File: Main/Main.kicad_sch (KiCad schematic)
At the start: 39 parts, among them J1 USB_B_Micro, SW1 SW_Push, SW2 SW_Push, U1 RP2350A-QFN60, U2 W25Q128JVS, U3 AMS1117-3.3, Y1 ABM8-272-T3

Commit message: moveSchematics
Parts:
- added C22: 1u, symbol Device:C
- added C23: 10u, symbol Device:C
- added C24: 0.1, symbol Device:C
- added C25, C26: 0.1uF, symbol Device:C
- added C27, C28: 100 nF, symbol Device:C
- added D1, D2: 100nF, symbol Device:D_Capacitance
- added H5, H6, H7, H8: pad, symbol Mechanical:MountingHole
- added R10, R11, R12, R13, R14: 4.7k, symbol Device:R
- added R7, R8: R, symbol Device:R
- added R9: 2m, symbol Device:R_Shunt
- added U10: LM75B, symbol Sensor_Temperature:LM75B
- added U4: MMC5983MA, MMC5983MA_MEM, symbol MMC5983MA:MMC5983MA
- added U5: ICM-42688-P, ICM-42688-P:PQFN50P300X250X97-14N, symbol ICM-42688-P:ICM-42688-P
- added U6: INA226, Package_SO:VSSOP-10_3x3mm_P0.5mm, symbol Sensor_Energy:INA226
- added U7: KX134-1211, LGA12_2X2X0P9_ROM, symbol KX134:KX134-1211
- added U8: MS5611-01BA, Package_LGA:LGA-8_3x5mm_P1.25mm, symbol Sensor_Pressure:MS5611-01BA
- added U9: RP2350A, Package_DFN_QFN:QFN-60-1EP_7x7mm_P0.4mm_EP3.4x3.4mm, symbol MCU_RaspberryPi:RP2350A
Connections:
- net +3.3V: now also C22.1, C24.1, R10.1, R11.1, R12.1, U4.13 (VDDIO), U4.2 (VDD), U6.6 (VS)
- net GND: now also C22.2, C23.2, C24.2, C25.2, C26.1, C27.2, C28.2, D1.2 (A), D2.2 (A), R9.4, U10.4 (GND), U10.5 (A2), U10.6 (A1), U10.7 (A0), U4.11 (GND), U4.9 (GND), U5.6 (GND), U5.7 (RESV_7), U6.1 (A1), U6.2 (A0), U6.7 (GND), U7.8 (GND), U7.9 (GND), U8.2 (PS), U8.3 (GND), U9.47 (VREG_PGND), U9.61 (GND)
- new net: R7.1, U5.14 (AP_SDA/AP_SDIO/AP_SDI)
- new net: D2.1 (K), R7.2, R8.2, U5.10 (RESV_10), U5.12 (AP_CS), U5.2 (RESV_2), U5.3 (RESV_3), U5.5 (VDDIO)
- new net: R13.2, U10.1 (SDA), U9.7 (GPIO4)
- new net: C23.1, U4.10 (CAP)
- new net: R9.2, U6.10 (Vin+)
- new net: R9.3, U6.8 (Vbus), U6.9 (Vin-)
- new net: D1.1 (K), U5.8 (VDD)
- new net: R8.1, U5.13 (AP_SCL/AP_SCLK)
- new net: R14.2, U10.2 (SCL), U9.8 (GPIO5)
- new net: U9.1 (IOVDD), U9.11 (IOVDD), U9.20 (IOVDD), U9.30 (IOVDD), U9.38 (IOVDD), U9.45 (IOVDD)
- new net: U9.23 (DVDD), U9.39 (DVDD), U9.6 (DVDD)
- new net +3V0: C27.1, U8.1 (VDD)
- new net +3V3: C28.1, R13.1, R14.1, U10.8 (+Vs), U9.49 (VREG_VIN)
- new net +7.5V: R9.1
- new net ACCEL_INT1: U7.5 (INT1)
- new net ACCEL_INT2: U7.6 (INT2)
- new net ACCEL_SCLK/SCL: U7.12 (SCLK/SCL)
- new net ACCEL_SDI/SDA: U7.2 (SDI/SDA)
- new net ACCEL_SDO/ADDR: U7.1 (SDO/ADDR)
- new net ACCEL_TRIG: U7.4 (TRIG)
- new net ACCEL_nCS: U7.10 (nCS)
- new net Alert: R12.2, U6.3 (~{Alert})
- new net Chip Select: U8.4 (CSB), U8.5 (CSB)
- new net I2C SCL: R11.2, U6.5 (SCL)
- new net I2C SDA: R10.2, U6.4 (SDA)
- new net IO_VDD: C25.1, U7.3 (IO_VDD)
- new net SCLK: U8.8 (SCLK)
- new net SCL/SPI_5CK: U4.1 (SCL/SPI_SCK)
- new net SDA/SPI_5DI: U4.16 (SDA/SPI_SDI)
- new net SDI: U8.7 (SDI/SDA)
- new net SDO: U8.6 (SDO)
- new net SPI_CS: U4.4 (SPI_CS)
- new net SPI_SD0: U4.5 (SPI_SDO)
- new net VDD: C26.2, U7.7 (VDD)

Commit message: Updated footprints
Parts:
- removed D1, D2: 100nF, symbol Device:D_Capacitance
- removed H5, H6, H7, H8: pad, symbol Mechanical:MountingHole
- removed R7, R8: R, symbol Device:R
- removed U5: ICM-42688-P, ICM-42688-P:PQFN50P300X250X97-14N, symbol ICM-42688-P:ICM-42688-P
- removed U9: RP2350A, Package_DFN_QFN:QFN-60-1EP_7x7mm_P0.4mm_EP3.4x3.4mm, symbol MCU_RaspberryPi:RP2350A
- C1, C2, C3, C4: footprint (none) -> Capacitor_SMD:C_0402_1005Metric
- C10, C11, C12, C13, C14, C15, C16, C17, C18, C19, C20, C21, C22, C23, C24, C25, C26, C27, C28, C5, C6, C7, C8, C9: footprint (none) -> Capacitor_SMD:C_0805_2012Metric
- L1: value 3.3u -> 3.3uH; footprint (none) -> Inductor_SMD:L_0805_2012Metric
- R1: footprint (none) -> Resistor_SMD:R_0402_1005Metric
- R10, R11, R12, R13, R14, R2, R3, R4, R5, R6: footprint (none) -> Resistor_SMD:R_0805_2012Metric
- U1: footprint (none) -> Package_DFN_QFN:QFN-60-1EP_7x7mm_P0.4mm_EP3.4x3.4mm
- U10: footprint (none) -> Package_SO:SOIC-8-1EP_3.9x4.9mm_P1.27mm_EP2.29x3mm
- U4: footprint MMC5983MA_MEM -> Package_LGA:LGA-16_3x3mm_P0.5mm
- U7: footprint LGA12_2X2X0P9_ROM -> Package_LGA:LGA-12_2x2mm_P0.5mm
- Y1: footprint (none) -> Crystal:Crystal_SMD_3225-4Pin_3.2x2.5mm
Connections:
- net SDA: now reaches R13.2, U10.1 (SDA)
- net SCL: now reaches R14.2, U10.2 (SCL)
- no-connect marks 1 -> 2
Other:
- moved on the sheet: C28, R13, R14, U10

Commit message: Fixes and Additions
Added current sensors for servos, fixed a few schematics for each chip, and made slight stylistic edits
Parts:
- removed R10, R11, R12, R13, R14: 4.7k, Resistor_SMD:R_0805_2012Metric, symbol Device:R
- added C29, C30, C31, C32, C33, C34: 100n, Capacitor_SMD:C_0805_2012Metric, symbol Device:C
- added R7, R8: 4.7k, Resistor_SMD:R_0805_2012Metric, symbol Device:R
- added U11, U12, U13, U9: MCS1802GS-50-Z, SOIC-8_MNP, symbol MCS1802:MCS1802GS-50-Z
- added U5: ICM-42688-P, ICM-42688-P:PQFN50P300X250X97-14N, symbol ICM-42688-P:ICM-42688-P
- C24: value 0.1 -> 100n
- C25, C26: value 0.1uF -> 100n
- C27, C28: value 100 nF -> 100n
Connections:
- net +3V0 is gone; now on net +3.3V: C27.1, U8.1 (VDD)
- net I2C SCL is gone; now on net SCL: U6.5 (SCL)
- net I2C SDA is gone; now on net SDA: U6.4 (SDA)
- net SCL/SPI_5CK is gone; now on net SPI_SCK: U4.1 (SCL/SPI_SCK)
- net +3.3V: now also C22.2, C29.1, C30.1, C31.1, C32.1, C33.1, C34.1, U11.8 (VCC), U12.8 (VCC), U13.8 (VCC), U5.10 (RESV_10), U5.2 (RESV_2), U5.3 (RESV_3), U5.5 (VDDIO), U5.8 (VDD), U9.8 (VCC); no longer C22.1
- net +3V3: now also R7.1, R8.1
- net GND: now also C22.1, C31.2, C32.2, C33.2, C34.2, U11.5 (GND), U12.5 (GND), U13.5 (GND), U5.6 (GND), U5.7 (RESV_7), U9.5 (GND); no longer C22.2
- net SCL: now also R8.2
- net SDA: now also R7.2
- net SPI_SD0: now also U5.1 (AP_SDO/AP_AD0)
- net +7.5V renamed VSS
- net ACCEL_SCLK/SCL renamed SPI_SCK
- net SPI_SCK: now also U5.13 (AP_SCL/AP_SCLK)
- net Chip Select renamed MS5611_CS
- net SDA/SPI_5DI renamed SPI_SDI
- net SPI_SDI: now also U5.14 (AP_SDA/AP_SDIO/AP_SDI)
- net SPI_CS renamed MMC_CS
- new net: C29.2, C30.2
- new net ICM_CS: U5.12 (AP_CS)
- new net INT2/DRDY: U5.9 (INT2/FSYNC/CLKIN)
- new net Vout1: U11.7 (VOUT)
- new net Vout2: U9.7 (VOUT)
- new net Vout3: U12.7 (VOUT)
- new net Vout4: U13.7 (VOUT)
- new net current +: U11.1 (IP+), U11.2 (IP+), U12.1 (IP+), U12.2 (IP+), U13.1 (IP+), U13.2 (IP+), U9.1 (IP+), U9.2 (IP+)
- new net current -1: U11.3 (IP-), U11.4 (IP-)
- new net current -2: U9.3 (IP-), U9.4 (IP-)
- new net current -3: U12.3 (IP-), U12.4 (IP-)
- new net current -4: U13.3 (IP-), U13.4 (IP-)
- no-connect marks 2 -> 9
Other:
- note added: "Connect Vout to analog in pin"
- note added: "I2C pullups"
- note added: "ICM-42688 6-Axis IMU"
- note added: "INA226 Power Sensor"
- note added: "KX134 High G Accelerometer"
- note added: "LM75B Temperature Sensor"
- note added: "MMC5983MA Magnetometer"
- note added: "MS5611 Barometer"
- note added: "Servo Current Sensing"
- moved on the sheet: C22, C24, C27, C28, R9, U10, U6, U8

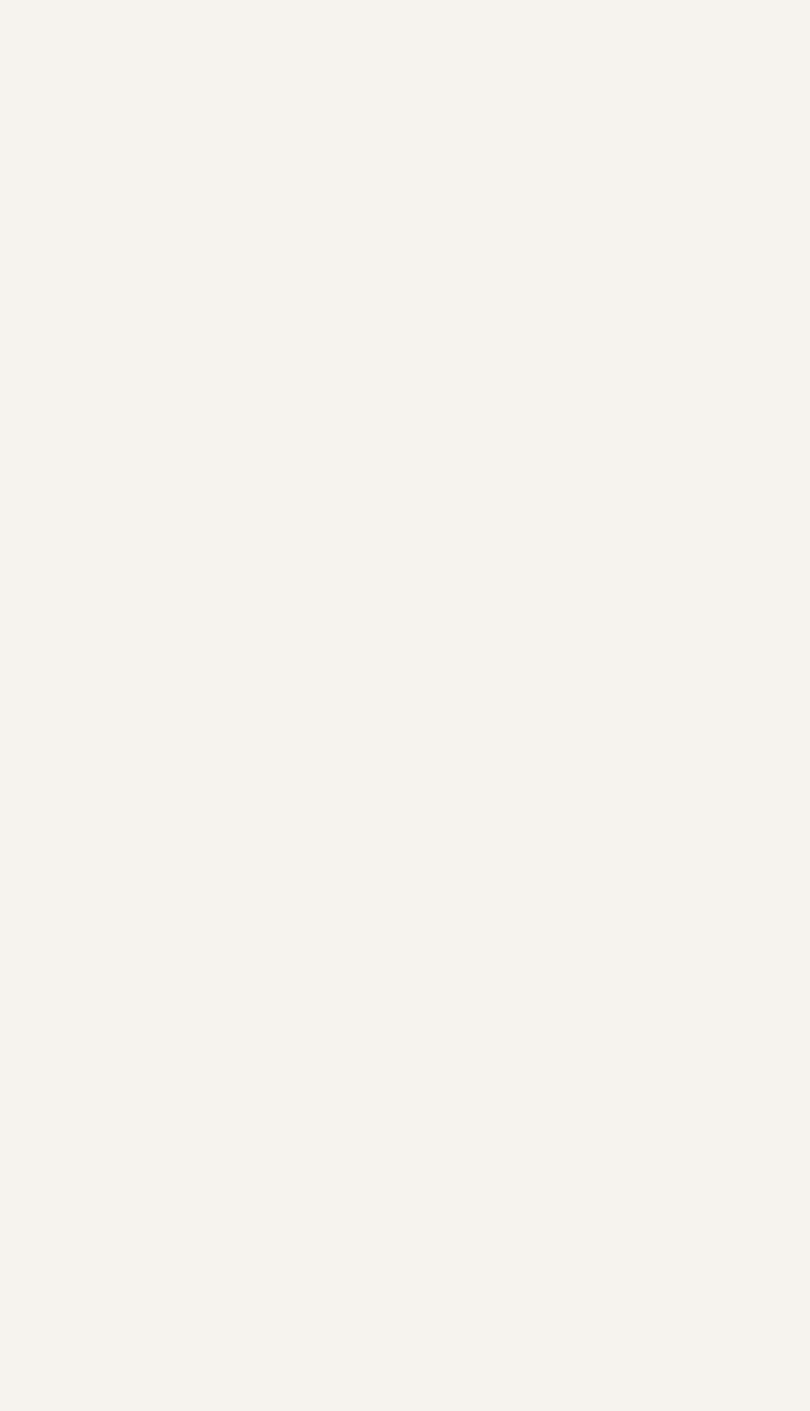
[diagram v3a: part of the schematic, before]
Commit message: Added servo connectors and micro SD
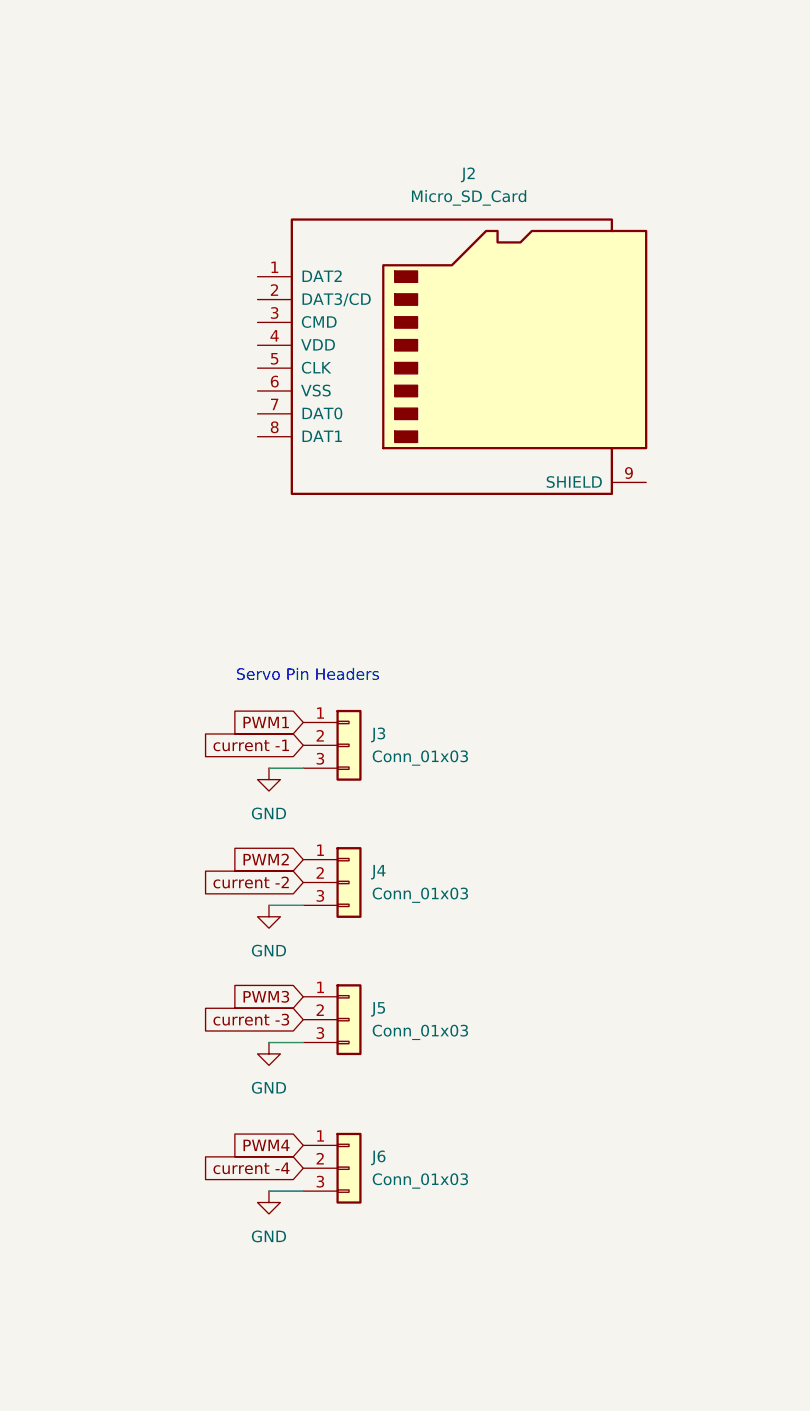
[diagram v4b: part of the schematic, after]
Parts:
- added J2: Micro_SD_Card, symbol Connector:Micro_SD_Card
- added J3, J4, J5, J6: Conn_01x03, symbol Connector_Generic:Conn_01x03
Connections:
- net GND: now also J3.3 (Pin_3), J4.3 (Pin_3), J5.3 (Pin_3), J6.3 (Pin_3)
- net current -1: now also J3.2 (Pin_2)
- net current -2: now also J4.2 (Pin_2)
- net current -3: now also J5.2 (Pin_2)
- net current -4: now also J6.2 (Pin_2)
- new net PWM1: J3.1 (Pin_1)
- new net PWM2: J4.1 (Pin_1)
- new net PWM3: J5.1 (Pin_1)
- new net PWM4: J6.1 (Pin_1)
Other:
- note added: "Servo Pin Headers"

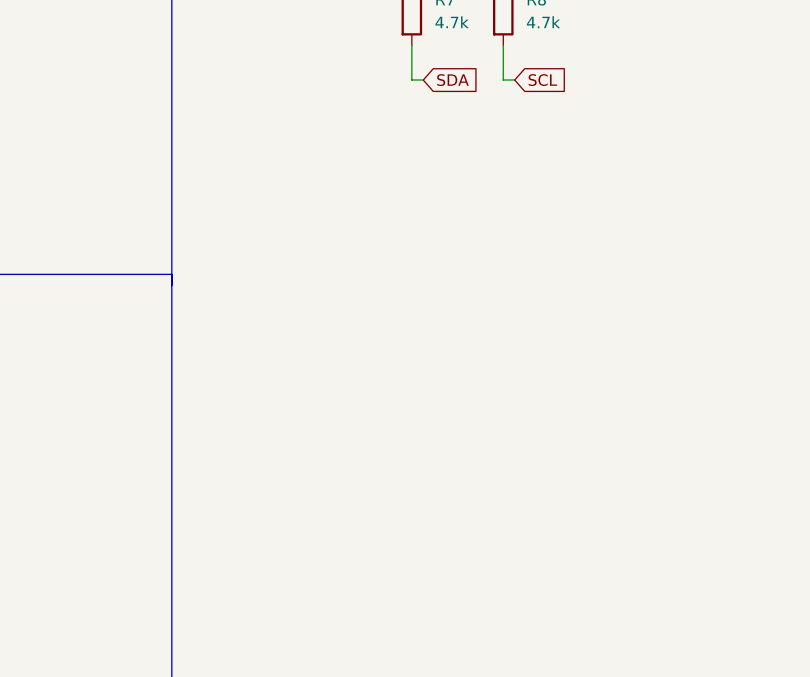
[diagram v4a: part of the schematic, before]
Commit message: added leds
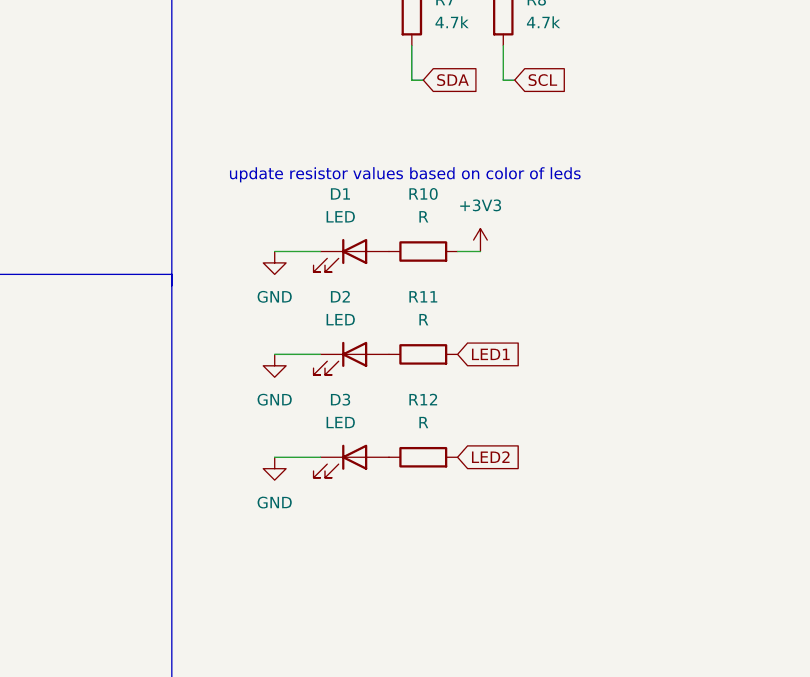
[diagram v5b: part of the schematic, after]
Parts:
- added D1, D2, D3: LED, LED_SMD:LED_0805_2012Metric, symbol Device:LED
- added R10, R11, R12: R, Resistor_SMD:R_0805_2012Metric, symbol Device:R
- J3, J4, J5, J6: footprint (none) -> Connector:FanPinHeader_1x03_P2.54mm_Vertical
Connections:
- net +3V3: now also R10.2
- net GND: now also D1.1 (K), D2.1 (K), D3.1 (K)
- new net: D2.2 (A), R11.1
- new net: D1.2 (A), R10.1
- new net: D3.2 (A), R12.1
- new net LED1: R11.2
- new net LED2: R12.2
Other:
- note added: "update resistor values based on color of leds"

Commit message: Started Layout
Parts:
- J3, J4, J5, J6: footprint Connector:FanPinHeader_1x03_P2.54mm_Vertical -> Connector_PinHeader_2.54mm:PinHeader_1x03_P2.54mm_Vertical
- U11, U12, U13, U9: footprint SOIC-8_MNP -> Package_SO:SOIC-8-1EP_3.9x4.9mm_P1.27mm_EP2.29x3mm
- U5: footprint ICM-42688-P:PQFN50P300X250X97-14N -> Package_LGA:LGA-14_3x2.5mm_P0.5mm_LayoutBorder3x4y
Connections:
- net current +: now also U12.3 (IP-), U12.4 (IP-), U9.3 (IP-), U9.4 (IP-); no longer U12.1 (IP+), U12.2 (IP+), U9.1 (IP+), U9.2 (IP+)
- net current -2: now also U9.1 (IP+), U9.2 (IP+); no longer U9.3 (IP-), U9.4 (IP-)
- net current -3: now also U12.1 (IP+), U12.2 (IP+); no longer U12.3 (IP-), U12.4 (IP-)
